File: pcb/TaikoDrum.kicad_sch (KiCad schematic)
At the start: 34 parts, among them J1 USB_B_Micro, J2 Conn_02x04_Odd_Even, U1 STM32F103C8Tx, U2 LM3940IMPX-3.3_NOPB, U3 LM358, Y1 8Mhz

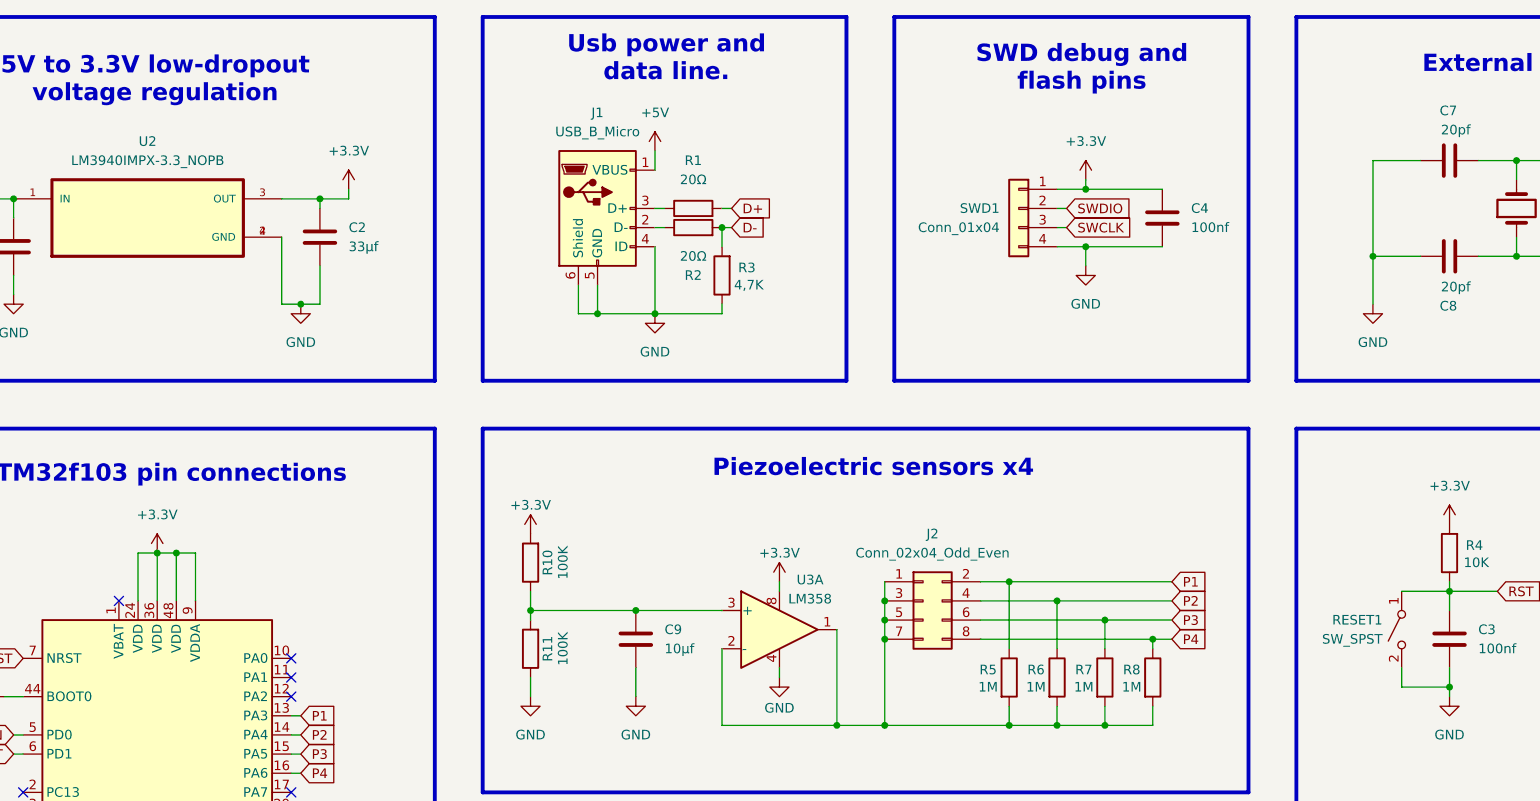
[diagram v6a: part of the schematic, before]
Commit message: Improved the schematic design with shared buffer for all four piezos and extra decoupling. Created first PCB design with all required components for THT soldering (except for STM32).
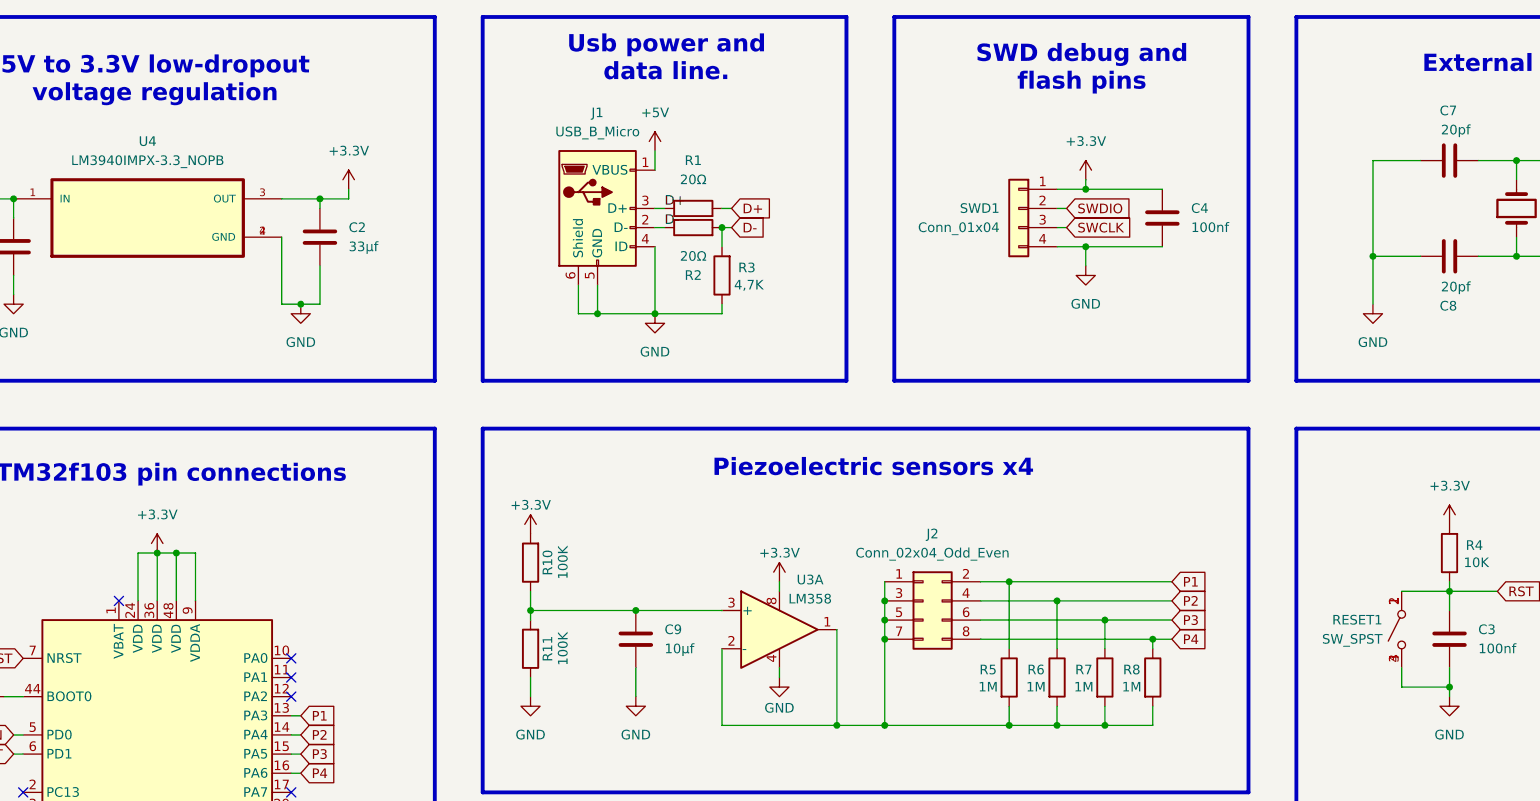
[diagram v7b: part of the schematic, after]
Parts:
- removed U2: LM3940IMPX-3.3_NOPB, LM3940IMPX-3.3_NOPB:SOT230P700X180-4N, symbol LM3940IMPX-3.3_NOPB:LM3940IMPX-3.3_NOPB
- added U4: LM3940IMPX-3.3_NOPB, LM3940IMPX-3.3_NOPB:SOT230P700X180-4N, symbol LM3940IMPX-3.3_NOPB:LM3940IMPX-3.3_NOPB
- C1, C2, C9: footprint Capacitor_SMD:C_0805_2012Metric_Pad1.18x1.45mm_HandSolder -> Capacitor_THT:C_Radial_D5.0mm_H5.0mm_P2.00mm
- RESET1: footprint (none) -> FSM8JH:SW_FSM8JH
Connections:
- net +3.3V: now also U4.3 (OUT)
- net +5V: now also U4.1 (IN)
- net D+: now also J1.3 (D+), R1.1
- net D-: now also J1.2 (D-), R2.1
- net GND: now also RESET1.3 (A), RESET1.4 (B), U4.2 (GND), U4.4 (GND); no longer RESET1.2 (B)
- net RST: now also RESET1.2 (B)
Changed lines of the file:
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@@
 	)
 	(junction
-		(at 35.56 43.18)
+		(at 167.64 113.03)
 		(diameter 0)
 		(color 0 0 0 0)
 	)
 	(junction
-		(at 167.64 113.03)
+		(at 76.2 43.18)
 		(diameter 0)
 		(color 0 0 0 0)
 	)
 	(junction
-		(at 76.2 43.18)
+		(at 35.56 43.18)
 		(diameter 0)
 		(color 0 0 0 0)
@@
 	(wire
 		(pts
-			(xy 120.65 44.45) (xy 121.92 44.45)
-		)
-		(stroke
-			(width 0)
-			(type default)
-		)
-	)
-	(wire
-		(pts
 			(xy 229.87 50.8) (xy 234.95 50.8)
 		)
@@
 	(wire
 		(pts
+			(xy 121.92 44.45) (xy 120.65 44.45)
+		)
+		(stroke
+			(width 0)
+			(type default)
+		)
+	)
+	(wire
+		(pts
 			(xy 151.13 96.52) (xy 151.13 99.06)
 		)
@@
 		)
 	)
+	(label "D+"
+		(at 121.92 44.45 0)
+		(effects
+			(font
+				(size 1.27 1.27)
+			)
+			(justify left bottom)
+		)
+	)
+	(label "D-"
+		(at 121.92 46.99 0)
+		(effects
+			(font
+				(size 1.27 1.27)
+			)
+			(justify left bottom)
+		)
+	)
 	(global_label "SWDIO"
 		(shape input)
@@
 			)
 		)
-		(property "Footprint" "Capacitor_SMD:C_0805_2012Metric_Pad1.18x1.45mm_HandSolder"
+		(property "Footprint" "Capacitor_THT:C_Radial_D5.0mm_H5.0mm_P2.00mm"
 			(at 77.1652 52.07 0)
 			(effects
@@
 	)
 	(symbol
+		(lib_name "LM3940IMPX-3.3_NOPB_1")
 		(lib_id "LM3940IMPX-3.3_NOPB:LM3940IMPX-3.3_NOPB")
 		(at 53.34 45.72 0)
@@
 		(dnp no)
 		(fields_autoplaced yes)
-		(property "Reference" "U2"
+		(property "Reference" "U4"
 			(at 53.34 35.56 0)
 			(effects
@@
 			)
 		)
-		(pin "1"
-		)
 		(pin "2"
 		)
 		(pin "3"
 		)
+		(pin "1"
+		)
 		(pin "4"
 		)
@@
 			(project ""
 				(path "/ee4ada02-05a0-4e49-92f9-f61a706c8588"
-					(reference "U2")
+					(reference "U4")
 					(unit 1)
 				)
@@
 			)
 		)
-		(property "Footprint" "Capacitor_SMD:C_0805_2012Metric_Pad1.18x1.45mm_HandSolder"
+		(property "Footprint" "Capacitor_THT:C_Radial_D5.0mm_H5.0mm_P2.00mm"
 			(at 34.5948 53.34 0)
 			(effects
@@
 			)
 		)
-		(property "Footprint" "Capacitor_SMD:C_0805_2012Metric_Pad1.18x1.45mm_HandSolder"
+		(property "Footprint" "Capacitor_THT:C_Radial_D5.0mm_H5.0mm_P2.00mm"
 			(at 119.0752 105.41 0)
 			(effects
@@
 			)
 		)
-		(property "Footprint" ""
+		(property "Footprint" "FSM8JH:SW_FSM8JH"
 			(at 219.71 100.33 0)
 			(effects
@@
 		(pin "2"
 		)
+		(pin "4"
+		)
+		(pin "3"
+		)
 		(instances

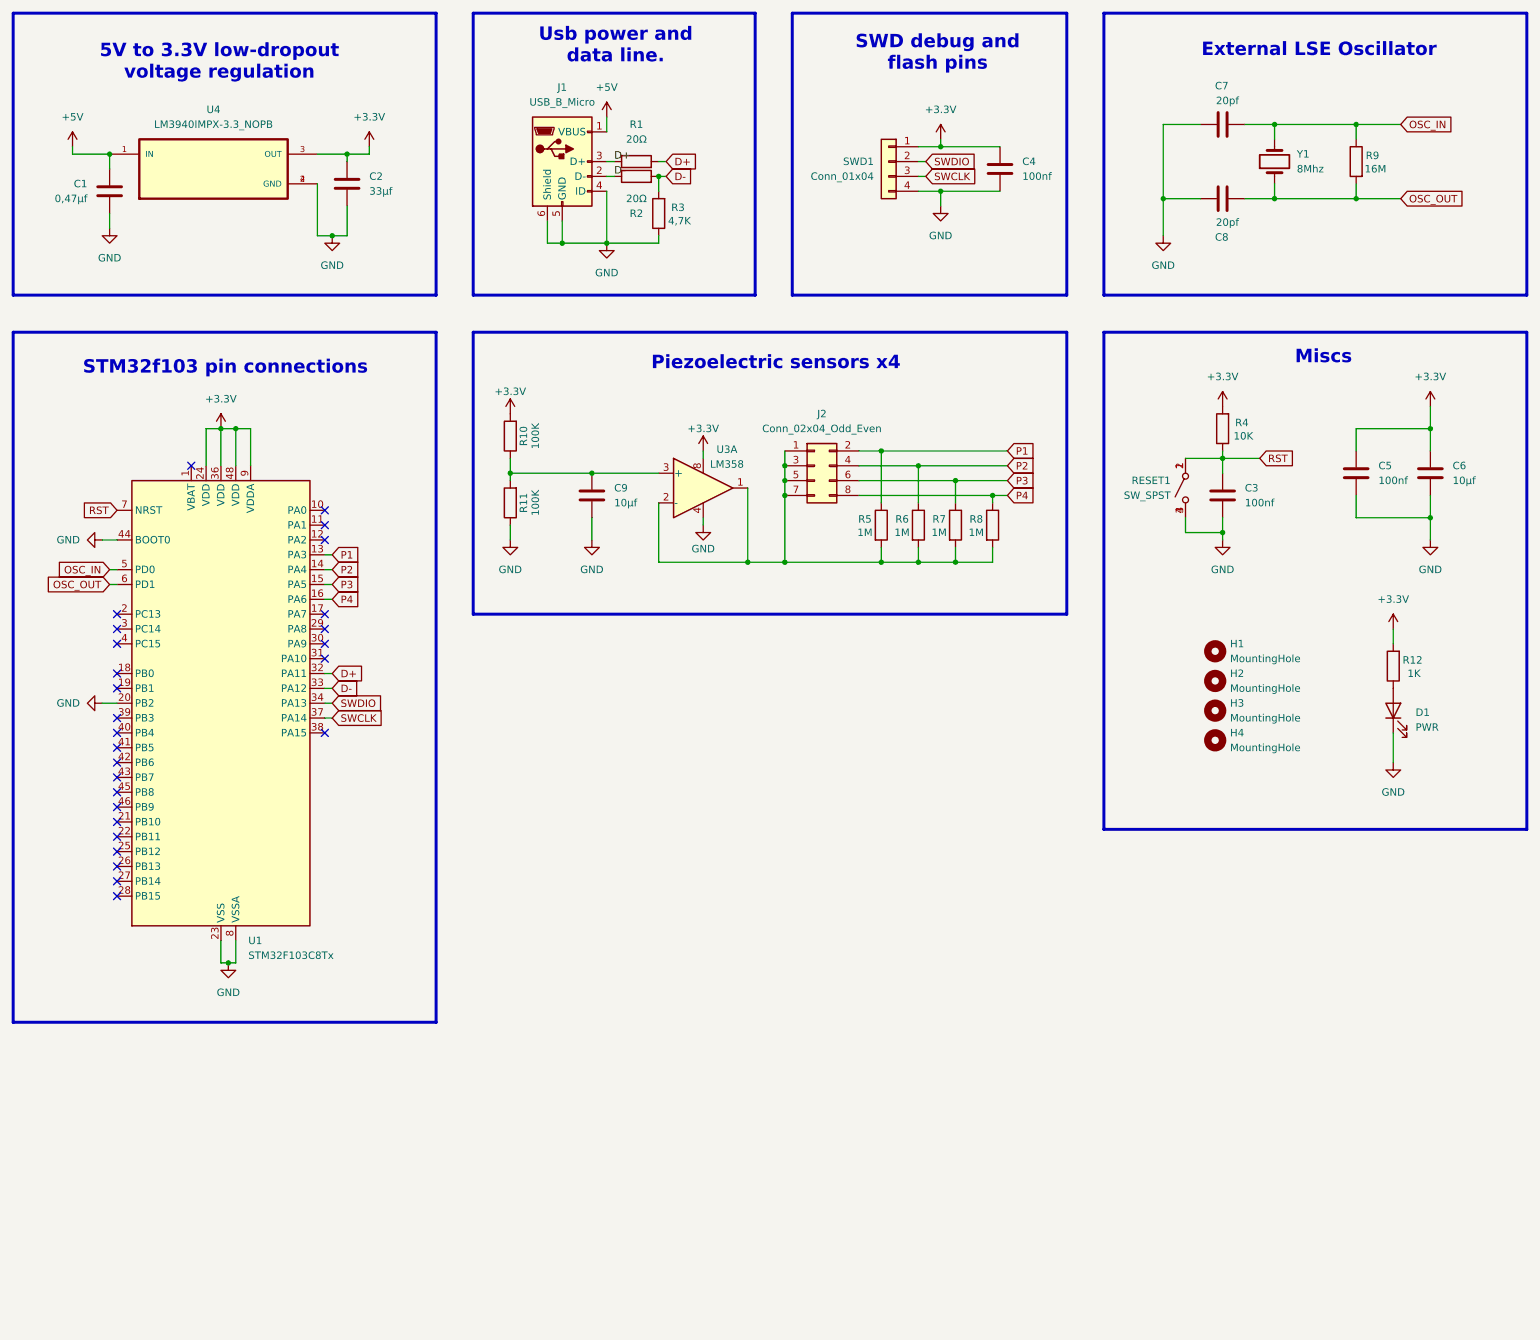
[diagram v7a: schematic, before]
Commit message: Fixed wrong USB wiring. Removed unecessary marks.
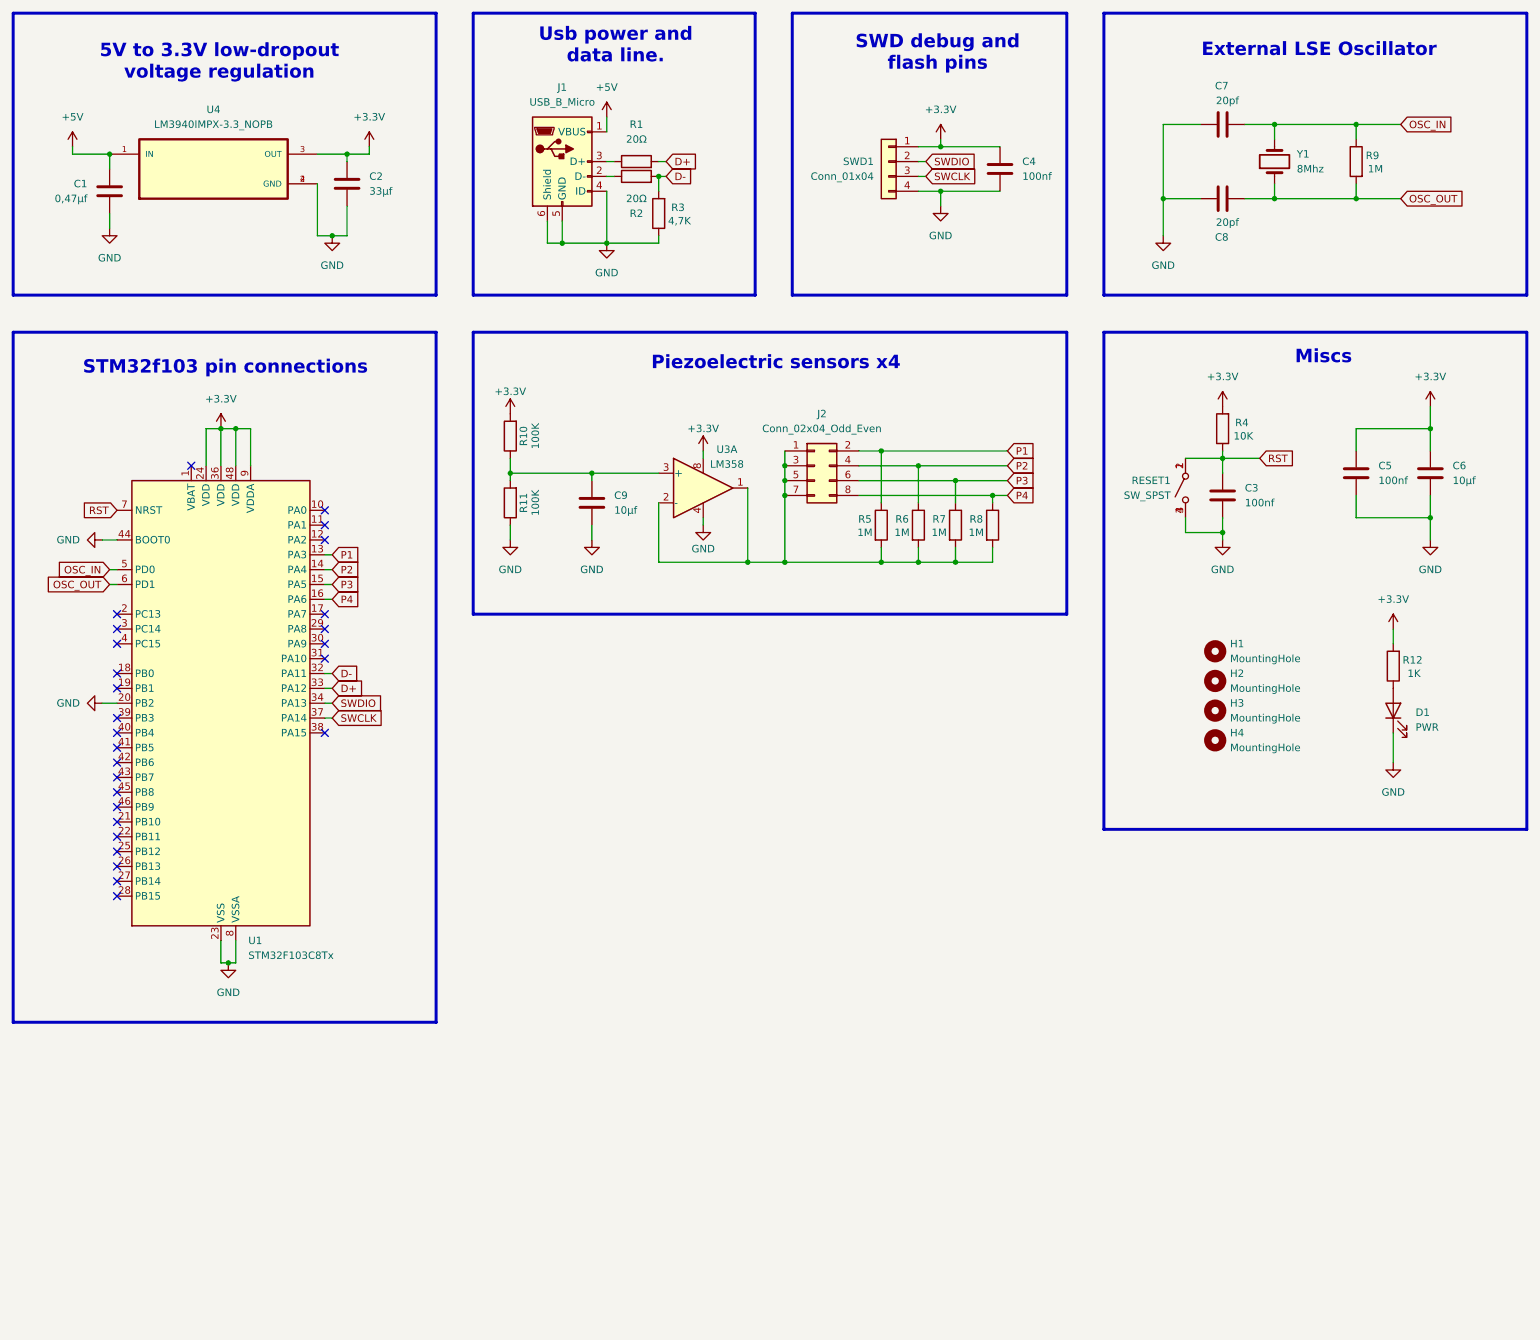
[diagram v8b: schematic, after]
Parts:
- R9: value 16M -> 1M
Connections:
- net D+: now also U1.33 (PA12); no longer J1.3 (D+), R1.1, U1.32 (PA11)
- net D-: now also U1.32 (PA11); no longer J1.2 (D-), R2.1, U1.33 (PA12)
- new net: J1.3 (D+), R1.1
- new net: J1.2 (D-), R2.1
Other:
- moved on the sheet: C9
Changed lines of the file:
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@@
 	(wire
 		(pts
-			(xy 118.11 109.22) (xy 118.11 105.41)
+			(xy 118.11 109.22) (xy 118.11 106.68)
 		)
 		(stroke
@@
 	(wire
 		(pts
-			(xy 72.39 134.62) (xy 73.66 134.62)
-		)
-		(stroke
-			(width 0)
-			(type default)
-		)
-	)
-	(wire
-		(pts
 			(xy 177.8 49.53) (xy 187.96 49.53)
 		)
@@
 	(wire
 		(pts
+			(xy 72.39 134.62) (xy 73.66 134.62)
+		)
+		(stroke
+			(width 0)
+			(type default)
+		)
+	)
+	(wire
+		(pts
 			(xy 121.92 44.45) (xy 120.65 44.45)
 		)
@@
 	(wire
 		(pts
+			(xy 118.11 99.06) (xy 118.11 97.79)
+		)
+		(stroke
+			(width 0)
+			(type default)
+		)
+	)
+	(wire
+		(pts
 			(xy 59.69 96.52) (xy 59.69 90.17)
 		)
@@
 		)
 	)
-	(label "D+"
-		(at 121.92 44.45 0)
-		(effects
-			(font
-				(size 1.27 1.27)
-			)
-			(justify left bottom)
-		)
-	)
-	(label "D-"
-		(at 121.92 46.99 0)
-		(effects
-			(font
-				(size 1.27 1.27)
-			)
-			(justify left bottom)
-		)
-	)
 	(global_label "SWDIO"
 		(shape input)
@@
 		)
 	)
+	(global_label "D+"
+		(shape input)
+		(at 73.66 134.62 0)
+		(fields_autoplaced yes)
+		(effects
+			(font
+				(size 1.27 1.27)
+			)
+			(justify left)
+		)
+		(property "Intersheetrefs" "${INTERSHEET_REFS}"
+			(at 79.4876 134.62 0)
+			(effects
+				(font
+					(size 1.27 1.27)
+				)
+				(justify left)
+				(hide yes)
+			)
+		)
+	)
 	(global_label "P2"
 		(shape input)
@@
 	(global_label "D-"
 		(shape input)
-		(at 73.66 134.62 0)
-		(fields_autoplaced yes)
-		(effects
-			(font
-				(size 1.27 1.27)
-			)
-			(justify left)
-		)
-		(property "Intersheetrefs" "${INTERSHEET_REFS}"
-			(at 79.4876 134.62 0)
-			(effects
-				(font
-					(size 1.27 1.27)
-				)
-				(justify left)
-				(hide yes)
-			)
-		)
-	)
-	(global_label "D+"
-		(shape input)
 		(at 73.66 132.08 0)
 		(fields_autoplaced yes)
@@
 	(symbol
 		(lib_id "Device:C")
-		(at 118.11 101.6 0)
+		(at 118.11 102.87 0)
 		(unit 1)
 		(exclude_from_sim no)
@@
 		(dnp no)
 		(property "Reference" "C9"
-			(at 121.92 100.3299 0)
+			(at 121.92 101.5999 0)
 			(effects
 				(font
@@
 		)
 		(property "Value" "10µf"
-			(at 121.92 102.8699 0)
+			(at 121.92 104.1399 0)
 			(effects
 				(font
@@
 		)
 		(property "Footprint" "Capacitor_THT:C_Radial_D5.0mm_H5.0mm_P2.00mm"
-			(at 119.0752 105.41 0)
+			(at 119.0752 106.68 0)
 			(effects
 				(font
@@
 		)
 		(property "Datasheet" "~"
-			(at 118.11 101.6 0)
+			(at 118.11 102.87 0)
 			(effects
 				(font
@@
 		)
 		(property "Description" "Unpolarized capacitor"
-			(at 118.11 101.6 0)
+			(at 118.11 102.87 0)
 			(effects
 				(font
@@
 			)
 		)
-		(property "Value" "16M"
+		(property "Value" "1M"
 			(at 252.222 45.72 0)
 			(effects
